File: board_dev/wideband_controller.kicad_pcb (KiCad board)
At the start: 2 copper layers, 35.7 x 34.2 mm, 55 parts, among them J1 Conn_02x05_Odd_Even, J2 Conn_01x06, J3 Conn_01x08, Q1 BTS3028, U1 MCP6004, U2 MCP6004, U4 STM32F042K6Ux, U9 XC6206P332MR

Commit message: cleanup & tweaks
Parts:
- R1: value 15k -> 10k
- R5, R7: value 30k -> 27k
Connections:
- U1 pad 11: +3V3 -> GND
- U1 pad 4: GND -> +3V3
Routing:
- net GND: track 3.63 -> 2.33 mm, vias 92 -> 93
- net /Ip_dac: track 11.1 -> 10.1 mm
- net /Ip_sense: track 15.6 -> 14.9 mm
- net /LSU_Rtrim: track 21.6 -> 22.2 mm
- net +3V3: track 79.6 -> 80.1 mm
- net Net-(R12-Pad1): track 8.36 -> 8.87 mm

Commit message: layout help from dave
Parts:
- added C16: 1u, Capacitor_SMD:C_0402_1005Metric, F.Cu at (105.3, 96.3)
- moved C2 2.99 mm to (97.4, 99.7), turned to 180 degrees
- moved R20 1.84 mm to (101.9, 99.7), turned to 90 degrees
- moved R22 1.55 mm to (100.3, 100.2)
- moved Q1 0.67 mm to (102.9, 76.6)
- moved C15 0.64 mm to (95.2, 84.8), turned to 90 degrees
- moved R13 0.64 mm to (94.1, 94.0)
- moved R18 0.38 mm to (104.9, 93.6)
- moved R3 0.30 mm to (95.8, 89.2)
- moved R7 0.27 mm to (95.8, 91.2)
- moved R19 0.25 mm to (105.3, 95.2)
- moved C3 0.16 mm to (96.8, 84.3)
- moved R8 0.07 mm to (96.8, 85.4)
- moved C12 0.07 mm to (91.7, 91.5)
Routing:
- net +3V3: track 80.1 -> 167.6 mm, vias 9 -> 8
- net /SWCLK: track 8.82 -> 25.8 mm, vias 2 -> 1
- net /SWDIO: track 9.73 -> 24.2 mm
- net Net-(C6-Pad2): track 6.57 -> 11.5 mm
- net Net-(C2-Pad2): track 6.06 -> 2.14 mm, vias 2 -> 0
- net /Ip_dac: track 10.1 -> 7.21 mm, vias 2 -> 0
- net Net-(R19-Pad1): track 5.65 -> 8.25 mm
- net Net-(R8-Pad2): track 5.23 -> 7.64 mm
- net /nRESET: track 11.0 -> 9.84 mm, vias 1 -> 2
- net /Vm: track 6.30 -> 7.32 mm
- net GND: track 2.33 -> 1.54 mm, vias 93 -> 101
- net /Un_sense: track 10.8 -> 11.6 mm
- net /LSU_Rtrim: track 22.2 -> 22.9 mm
- net /LSU_Un: track 19.4 -> 18.9 mm
- net /LSU_Un_sense: track 56.8 -> 56.2 mm, vias 3 -> 5
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- added copper zone on B.Cu, net /LSU_Un_sense

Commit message: pcb tweakery
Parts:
- removed C15: 100n, Capacitor_SMD:C_0402_1005Metric
- removed R28: 3.3k, Resistor_SMD:R_0402_1005Metric
- added R31: 68k, Resistor_SMD:R_0402_1005Metric, F.Cu at (92.8, 84.8)
- added R32: 68k, Resistor_SMD:R_0402_1005Metric, F.Cu at (97.3, 85.1)
- added R33: 10k, Resistor_SMD:R_0402_1005Metric, F.Cu at (94.2, 84.8)
- added R34: 10k, Resistor_SMD:R_0402_1005Metric, F.Cu at (96.3, 84.5)
- C3: value 100n -> 33n
- C6: value 3.3n -> 1n
- R16: value 10k -> 3.3k
- R6: value 20k -> 22k
- R8: value 10 -> 47
- moved C3 3.33 mm to (93.6, 83.3)
- moved R8 1.73 mm to (95.2, 84.6), turned to 270 degrees
- moved R10 0.25 mm to (98.6, 84.2)
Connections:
- C11 pad 1: Net-(C11-Pad1) -> /Ip_sense
- C3 pad 1: /LSU_Rtrim -> Net-(C3-Pad1)
- C3 pad 2: GND -> Net-(C3-Pad2)
- R17 pad 1: /Ip_sense -> Net-(R17-Pad1)
- R24 pad 1: /Ip_sense -> Net-(R17-Pad1)
- R24 pad 2: Net-(C11-Pad1) -> /Ip_sense
- R8 pad 2: Net-(R8-Pad2) -> Net-(C3-Pad1)
- U1 pad 1: Net-(R8-Pad2) -> Net-(C3-Pad1)
- U1 pad 2: Net-(R8-Pad2) -> Net-(C3-Pad2)
- U1 pad 3: /Ip_dac -> Net-(R32-Pad1)
- U1 pad 8: /Ip_sense -> Net-(R17-Pad1)
- U4 pad 12: Net-(R28-Pad2) -> /Ip_dac
- U4 pad 8: Net-(C11-Pad1) -> /Ip_sense
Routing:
- net Net-(R17-Pad1): track 0.00 -> 14.4 mm, vias 0 -> 2
- net /Ip_sense: track 14.4 -> 3.90 mm, vias 2 -> 0
- net Net-(R8-Pad2): track 7.64 -> 0.00 mm
- net Net-(C3-Pad2): track 0.00 -> 7.35 mm
- net /Vm: track 7.32 -> 14.2 mm, vias 0 -> 2
- net Net-(R32-Pad1): track 0.00 -> 5.80 mm
- net Net-(C3-Pad1): track 0.00 -> 5.69 mm
- net Net-(R28-Pad2): track 4.30 -> 0.00 mm
- net Net-(C11-Pad1): track 3.90 -> 0.00 mm
- net /Ip_dac: track 7.21 -> 4.88 mm
- net /LSU_Rtrim: track 22.9 -> 25.1 mm
- net GND: vias 101 -> 102

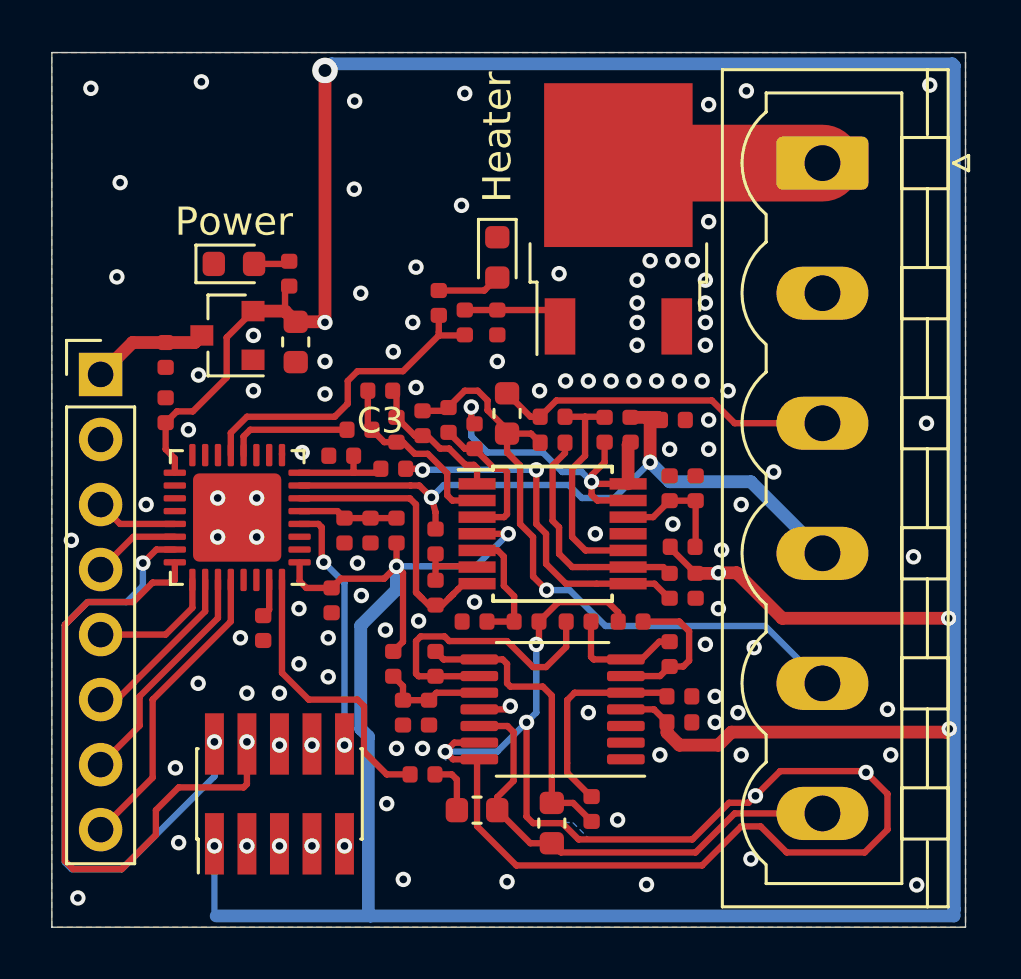
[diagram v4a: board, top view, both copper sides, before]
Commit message: switch to 14 pin stlinkv3 connector
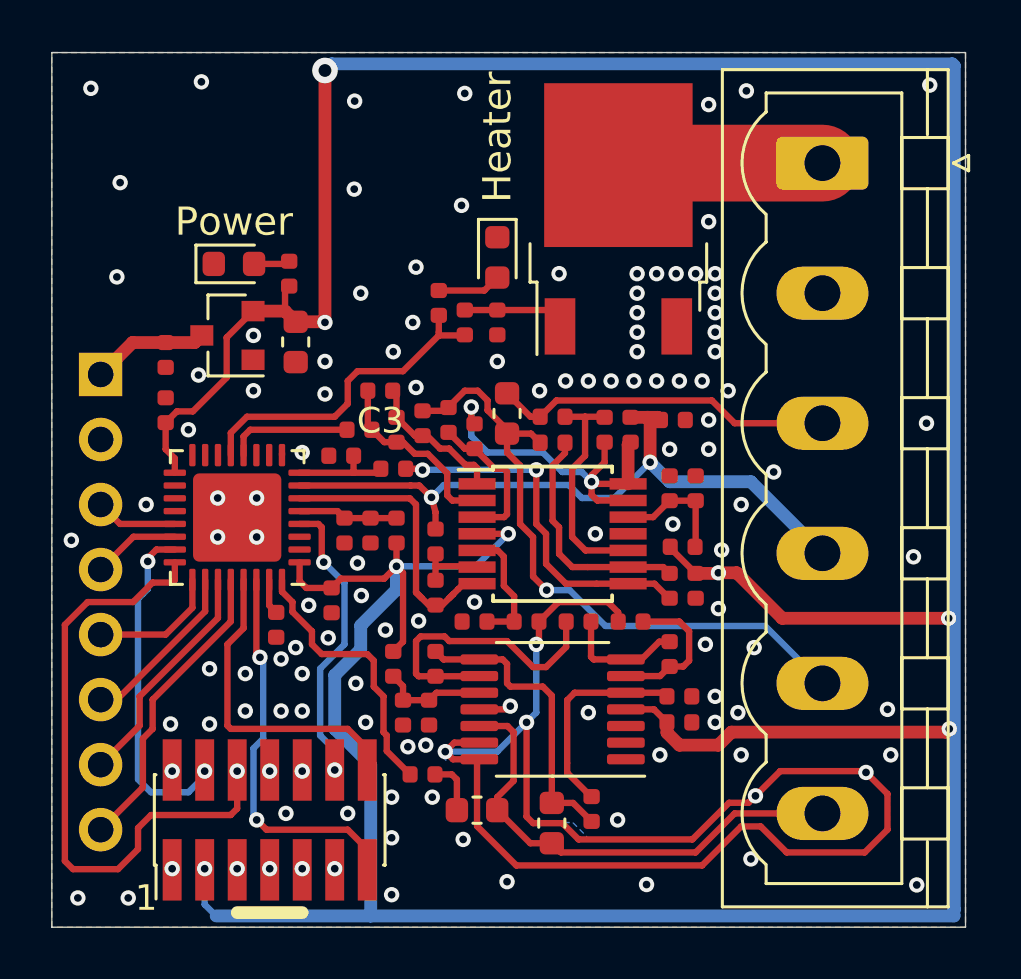
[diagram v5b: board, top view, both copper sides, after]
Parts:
- removed J1: Conn_02x05_Odd_Even, Connector_PinHeader_1.27mm:PinHeader_2x05_P1.27mm_Vertical_SMD
- added J4: FTSH-107-01-F-DV-K, Connector_PinHeader_1.27mm:PinHeader_2x07_P1.27mm_Vertical_SMD, F.Cu at (89.3, 100.1)
- J3: moved to B.Cu
- moved R29 0.52 mm to (89.5, 92.5)
- turned J3 to 180 degrees
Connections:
- U4 pad 29: Net-(U4-Pad29) -> /UART_TX
- U4 pad 30: Net-(U4-Pad30) -> /UART_RX
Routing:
- net /UART_RX: track 0.00 -> 15.3 mm, vias 0 -> 2
- net /UART_TX: track 0.00 -> 12.6 mm
- net /SWDIO: track 24.2 -> 13.3 mm
- net /nRESET: track 9.84 -> 11.4 mm
- net /SWCLK: track 25.8 -> 24.8 mm
- net /Nernst_esr_drive: track 11.3 -> 10.7 mm
- net GND: track 1.54 -> 1.43 mm, vias 102 -> 114
- net Net-(J1-Pad7): track 0.08 -> 0.00 mm, vias 1 -> 0
- net Net-(J4-Pad9): track 0.00 -> 0.05 mm, vias 0 -> 1
- net Net-(J4-Pad8): track 0.00 -> 0.05 mm, vias 0 -> 1
- net Net-(J4-Pad2): track 0.00 -> 0.05 mm, vias 0 -> 1
- net Net-(J4-Pad10): track 0.00 -> 0.05 mm, vias 0 -> 1
- net Net-(J4-Pad1): track 0.00 -> 0.05 mm, vias 0 -> 1
- net Net-(J1-Pad8): track 0.05 -> 0.00 mm, vias 1 -> 0
- net Net-(J1-Pad6): track 0.05 -> 0.00 mm, vias 1 -> 0
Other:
- board text added: "1"
